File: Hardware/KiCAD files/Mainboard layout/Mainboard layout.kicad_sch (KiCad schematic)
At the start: 104 parts, among them J1 Conn_01x02, J10 Conn_01x02, J14 Conn_01x03, J15 Conn_01x03, J2 Conn_01x06, J28 Conn_01x03, J3 Conn_01x02, J30 USB-A1VSB6, J31 JST_03, J33 Conn_01x04, J34 JST_03, J35 JST_03, J36 JST_03, J37 JST_03, J38 JST_03, J39 JST_03, J4 Conn_01x06, J5 Conn_01x04, J6 Conn_01x06, J7 Conn_01x06, J8 Conn_01x06, J9 Conn_01x10, Q2 2DD1664, Q4 2N7000, SW8 Push_Button, SW9 Push_Button, U10 DRV8825PWPR, U12 ESP32-S3-WROOM-1, U3 PCA9534PW, U4 DRV8825PWPR, U8 DRV8825PWPR, U9 DRV8825PWPR

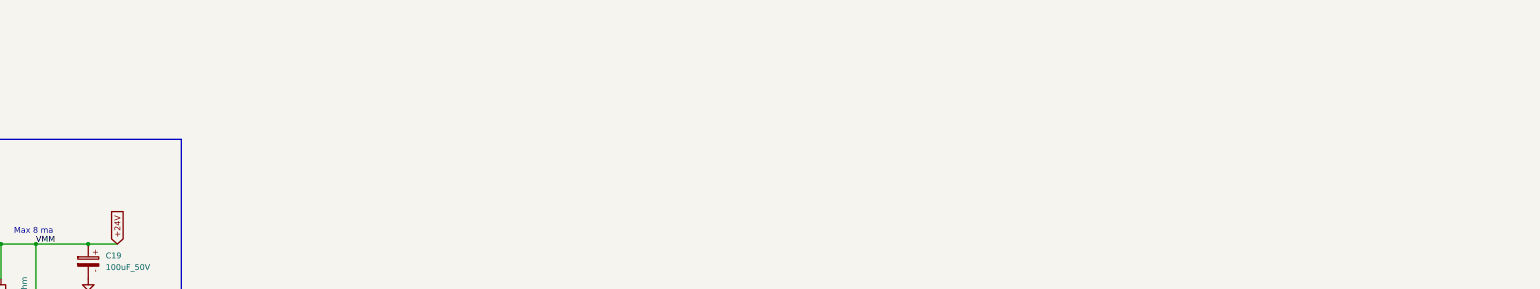
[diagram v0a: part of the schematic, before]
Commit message: Layout start
Was having issues with assigning pinouts on my initial schematics due to missing footprints, layouts broken into different schematics.
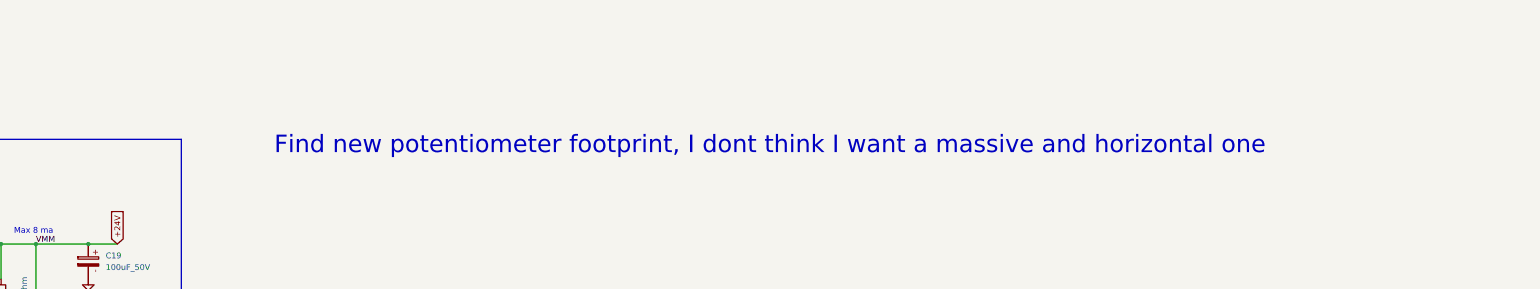
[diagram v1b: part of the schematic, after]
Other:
- note added: "Find new potentiometer footprint, I dont think I want a massive and horizontal one"
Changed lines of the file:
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@@
+		)
+	)
+	(text "Find new potentiometer footprint, I dont think I want a massive and horizontal one"
+		(exclude_from_sim no)
+		(at 480.314 294.64 0)
+		(effects
+			(font
+				(size 3.81 3.81)
+			)
 		)
 	)

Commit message: Mainboard Layout V1
completed Mainboard V1 layout and one swapping side, a hotfix to come of the other board to take swapping side
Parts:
- removed C10, C11, C13, C14, C15, C31, C32, C36, C39, C40, C44, C9: 0.1uF, PCM_SparkFun-Capacitor:C_0603_1608Metric, symbol PCM_SparkFun-Capacitor:0.1uF_0603_100V_10%
- removed C12, C19, C37, C45: 100uF_50V, Capacitor_THT:CP_Radial_D8.0mm_P3.50mm, symbol PCM_SL_Capacitors:100uF_50V
- removed C17, C18, C30, C38: 4.7uF, PCM_SparkFun-Capacitor:C_0603_1608Metric, symbol PCM_SparkFun-Capacitor:4.7uF_0603_35V_20%
- removed C20, C27, C33, C41: 470nF, PCM_SparkFun-Capacitor:C_0402_1005Metric, symbol PCM_SparkFun-Capacitor:470nF_0402_25V_10%
- removed C21, C28, C34, C42: 10nF, PCM_SparkFun-Capacitor:C_0603_1608Metric, symbol PCM_SparkFun-Capacitor:10nF_0603_50V_10%
- removed C22, C29, C35, C43: 0.1uF, PCM_SparkFun-Capacitor:C_0603_1608Metric, symbol PCM_SparkFun-Capacitor:0.1uF_0603_25V_20%
- removed J2, J4, J6, J7: Conn_01x06, PCM_SparkFun-Connector:1x06_P2.54mm, symbol PCM_SparkFun-Connector:Conn_01x06_P2.54mm
- removed J3: Conn_01x02, PCM_SparkFun-Connector:1x02_P2.54mm, symbol PCM_SparkFun-Connector:Conn_01x02_P2.54mm
- removed J33: Conn_01x04, PCM_SparkFun-Connector:1x04_P2.54mm, symbol PCM_SparkFun-Connector:Conn_01x04_P2.54mm
- removed Q4: 2N7000, PCM_Package_TO_SOT_THT_AKL:TO-92_Inline_Wide_SGD, symbol PCM_Transistor_MOSFET_AKL:2N7000
- removed R10, R19, R24, R29: 1.5k, PCM_SparkFun-Resistor:R_0603_1608Metric, symbol PCM_SparkFun-Resistor:1.5k_0603
- removed R11, R21, R26, R31: 10k Linear, PCM_SparkFun-Resistor:Bourns-PDB18, symbol PCM_SparkFun-Resistor:Trimpot_10k_RA_PTH
- removed R12, R22, R27, R32: 10k, PCM_SparkFun-Resistor:R_0603_1608Metric, symbol PCM_SparkFun-Resistor:10k_0603
- removed R16, R20, R25, R30: 1_Mohm, symbol PCM_Resistor_AKL:R_Generic
- removed R23, R28, R4, R9: .2 ohm, symbol PCM_Resistor_AKL:R_Generic
- removed R37, R38: 10k, Resistor_THT:R_Axial_DIN0207_L6.3mm_D2.5mm_P10.16mm_Horizontal, symbol PCM_SL_Resistors:10k
- removed U10, U4, U8, U9: DRV8825PWPR, symbol DRV8825PRPR driver chip:DRV8825PWPR
- added C23: 0.1uF, PCM_SparkFun-Capacitor:C_0603_1608Metric, symbol PCM_SparkFun-Capacitor:0.1uF_0603_25V_20%
- added J11, J17, J19, J21, J23, J24, J25, J26: Conn_01x06, PCM_SparkFun-Connector:1x06_P2.54mm, symbol PCM_SparkFun-Connector:Conn_01x06_P2.54mm
- added J12, J4, J6, J7: JST_06, Connector_JST:JST_EH_B6B-EH-A_1x06_P2.50mm_Vertical, symbol PCM_SL_Connectors:JST_06
- added J13: Conn_01x08, PCM_SparkFun-Connector:1x08_P2.54mm, symbol PCM_SparkFun-Connector:Conn_01x08_P2.54mm
- added J2: Screw_Terminal_2_P5.00mm, TerminalBlock_Phoenix:TerminalBlock_Phoenix_PT-1,5-2-5.0-H_1x02_P5.00mm_Horizontal, symbol PCM_SL_Screw_Terminal:Screw_Terminal_2_P5.00mm
- added J22, J29: Conn_01x03, PCM_SparkFun-Connector:1x03_P2.54mm, symbol PCM_SparkFun-Connector:Conn_01x03_P2.54mm
- added J3: Screw_Terminal_2_P3.50mm, TerminalBlock_Phoenix:TerminalBlock_Phoenix_PT-1,5-2-3.5-H_1x02_P3.50mm_Horizontal, symbol PCM_SL_Screw_Terminal:Screw_Terminal_2_P3.50mm
- added Q5: 2N7000, PCM_Package_TO_SOT_THT_AKL:TO-92_Inline_Wide_SGD, symbol PCM_Transistor_MOSFET_AKL:2N7000
- added R1: 1k, Resistor_THT:R_Axial_DIN0207_L6.3mm_D2.5mm_P10.16mm_Horizontal, symbol PCM_SL_Resistors:1k
- added R39: 10k, Resistor_THT:R_Axial_DIN0207_L6.3mm_D2.5mm_P10.16mm_Horizontal, symbol PCM_SL_Resistors:10k
- added R40: 100k, Resistor_THT:R_Axial_DIN0207_L6.3mm_D2.5mm_P10.16mm_Horizontal, symbol PCM_SL_Resistors:10k
- added R54: 10k, PCM_SparkFun-Resistor:R_0603_1608Metric, symbol PCM_SparkFun-Resistor:10k_0603
- added U5: PCA9534PW, PCM_SparkFun-Semiconductor-Standard:TSSOP-16_4.4x5mm_P0.65mm, symbol PCM_SparkFun-IC-Special-Function:PCA9534PW
- J1: value Conn_01x02 -> Programmer pins Conn_01x02
- J30: footprint USB-A1VSB6:ONSHORE_USB-A1VSB6 -> Connector_USB:USB_A_Kycon_KUSBX-AS1N-B_Horizontal
- R107, R89, R90, R91: footprint Resistor_SMD:R_0402_1005Metric_Wbry -> PCM_SparkFun-Resistor:R_0603_1608Metric
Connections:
- net SPI4_SCK is gone; now on net SPI4_CLK: J8.1 (Pin_1)
- net VBUS is gone; now on net +5V_HIGHPW: J30.1 (VUSB)
- net +24V: now also J2.1, J22.3 (Pin_3), J29.3 (Pin_3)
- net +3.3V: now also C23.1, J13.3 (Pin_3), J22.1 (Pin_1), Q5.2 (G), R54.1, U5.8 (VSS)
- net +5V: now also R40.2
- net DRIVER_0_STEP: now also J23.2 (Pin_2), J24.2 (Pin_2), J25.2 (Pin_2), J26.2 (Pin_2), R1.1
- net GND: now also C23.2, J13.2 (Pin_2), J2.2, J22.2 (Pin_2), J29.2 (Pin_2), J3.2, R39.2, U5.1 (A0), U5.16 (VDD), U5.2 (A1); no longer U12.15 (GPIO3/TOUCH3/ADC1_CH2)
- net IO_Interupter: now also U5.13 (~{INT})
- net MISO_1: now also J13.7 (Pin_7); no longer J5.2 (Pin_2)
- net MODE_0_GPIO: now also U3.4 (IO0), J23.5 (Pin_5), J24.5 (Pin_5), J25.5 (Pin_5); no longer U3.6 (IO2)
- net MODE_0_GPIOE: now also J26.5 (Pin_5)
- net MODE_1_GPIO: now also J23.4 (Pin_4), J24.4 (Pin_4), J25.4 (Pin_4)
- net MODE_1_GPIOE: now also J26.4 (Pin_4)
- net MODE_2_GPIO: now also U3.6 (IO2), J23.3 (Pin_3), J24.3 (Pin_3), J25.3 (Pin_3); no longer U3.4 (IO0)
- net MODE_2_GPIOE: now also J26.3 (Pin_3)
- net N_ENBL: now also J23.6 (Pin_6), J24.6 (Pin_6), J25.6 (Pin_6), J26.6 (Pin_6)
- net SPI1_CLK: now also J13.4 (Pin_4)
- net SPI1_CS: now also J13.6 (Pin_6)
- net SSR_Switch: now also J3.1, Q5.3 (D), R40.1
- net TEMP_HOTPLATE: no longer U12.39 (GPIO1/TOUCH1/ADC1_CH0)
- net TX: now reaches J1.1 (Pin_1), U12.37 (U0TXD/GPIO43/CLK_OUT1)
- net RX: now reaches J1.2 (Pin_2), U12.36 (U0RXD/GPIO44/CLK_OUT2)
- net at R53.1, U12.8 (GPIO15/U0RTS/ADC2_CH4/XTAL_32K_P), U3.15 (SDA): now also U5.15 (SDA)
- net at R52.1, U12.9 (GPIO16/U0CTS/ADC2_CH5/XTAL_32K_N), U3.14 (SCL): now also U5.14 (SCL)
- net DRDY_ALOW: now reaches U12.34 (MTDI/GPIO41/CLK_OUT1)
- net DRDY_ALOW: now also J13.8 (Pin_8)
- net TFT_interrupt: now reaches U12.35 (MTMS/GPIO42)
- net DIR: no longer names the net of U12.16 (GPIO46)
- new net: R54.2, U5.3 (A2)
- new net +12V: J29.1 (Pin_1)
- new net 3.3V_in1: Q5.1 (S), R39.1, U12.15 (GPIO3/TOUCH3/ADC1_CH2)
- new net A1_DRV0: J11.6 (Pin_6), J4.6
- new net A1_DRV1: J17.6 (Pin_6), J6.6
- new net A1_DRV2: J19.6 (Pin_6), J7.6
- new net A1_DRV3: J12.6, J21.6 (Pin_6)
- new net A2_DRV0: J11.3 (Pin_3), J4.3
- new net A2_DRV1: J17.3 (Pin_3), J6.3
- new net A2_DRV2: J19.3 (Pin_3), J7.3
- new net A2_DRV3: J12.3, J21.3 (Pin_3)
- new net B1_DRV0: J11.4 (Pin_4), J4.4
- new net B1_DRV1: J17.4 (Pin_4), J6.4
- new net B1_DRV2: J19.4 (Pin_4), J7.4
- new net B1_DRV3: J12.4, J21.4 (Pin_4)
- new net B2_DRV0: J11.1 (Pin_1), J4.1
- new net B2_DRV1: J17.1 (Pin_1), J6.1
- new net B2_DRV2: J19.1 (Pin_1), J7.1
- new net B2_DRV3: J12.1, J21.1 (Pin_1)
- new net CHAINL0_MISO_1: J13.5 (Pin_5), J5.2 (Pin_2)
- new net DIR0: J23.1 (Pin_1), U5.4 (IO0)
- new net DIR1: J24.1 (Pin_1), U5.5 (IO1)
- new net DIR2: J25.1 (Pin_1), U5.6 (IO2)
- new net DIR3: J26.1 (Pin_1), U5.7 (IO3)
- new net STEP: R1.2
- no-connect marks 31 -> 28
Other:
- note added: "may want to have parralel interrupts"
- note removed: "A1-A2, B1-B2 phases for stepper motors"
- note removed: "ALL NOTES FOR MOTOR DRIVER SCHEM"
- note removed: "DRV8825 1.1 D0"
- note removed: "DRV8825 1.1 D02"
- note removed: "DRV8825 1.1 D03 Extruder"
- note removed: "DRV8825 1.1 D1"
- note removed: "Find new potentiometer footprint, I dont think I want a massive and horizontal one"
- note removed: "Max 8 ma"
- note removed: "NoteMeausure impedance of the lines in layout ISA and ISB are .20 ohm, do with wire parasitics"
- note removed: "Replace all generics for specific componenets"
- note removed: "SLP @ fault"
- note removed: "This is designed to be integrated only leaving a connector output to the stepper"
- note removed: "Verify the coil Physically"
- moved on the sheet: J14, J15, J28

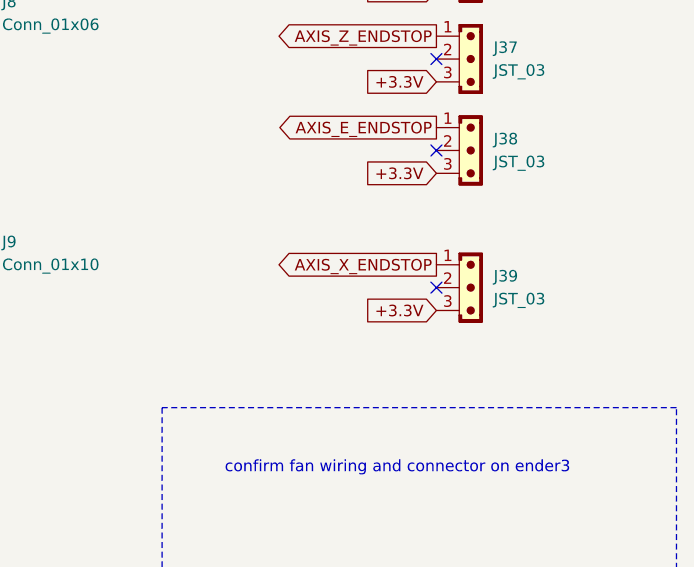
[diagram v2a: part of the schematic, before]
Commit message: Hotfix to create non-swapping board
hotfix on non-swapping done, swapping board is mapped for completion after CAD modeling phase begins
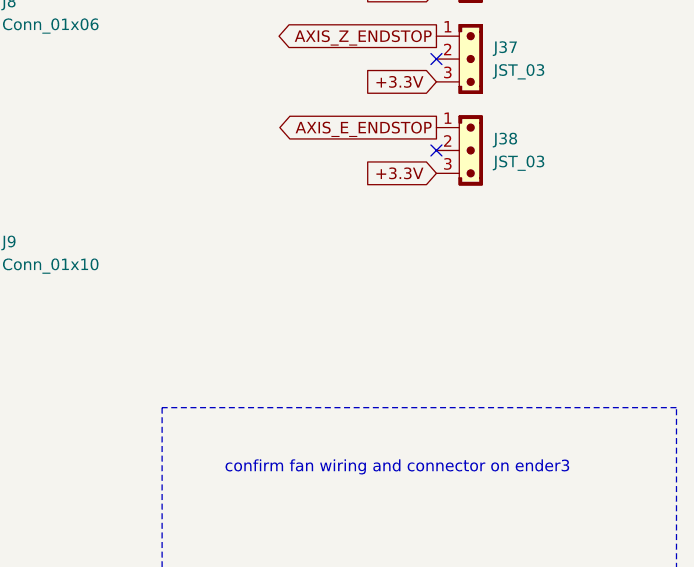
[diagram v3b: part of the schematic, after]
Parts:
- removed J39: JST_03, Connector_JST:JST_EH_B3B-EH-A_1x03_P2.50mm_Vertical, symbol PCM_SL_Connectors:JST_03
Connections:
- no-connect marks 28 -> 27
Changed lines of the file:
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@@
 	)
 	(no_connect
-		(at 797.56 91.44)
-	)
-	(no_connect
 		(at 797.56 45.72)
 	)
@@
 		)
 	)
-	(global_label "AXIS_X_ENDSTOP"
-		(shape output)
-		(at 797.56 88.9 180)
-		(fields_autoplaced yes)
-		(effects
-			(font
-				(size 1.27 1.27)
-			)
-			(justify right)
-		)
-		(property "Intersheetrefs" "${INTERSHEET_REFS}"
-			(at 778.7906 88.9 0)
-			(hide yes)
-			(show_name no)
-			(do_not_autoplace no)
-			(effects
-				(font
-					(size 1.27 1.27)
-				)
-				(justify right)
-			)
-		)
-	)
 	(global_label "SSR_Switch"
 		(shape input)
@@
 		)
 	)
-	(global_label "+3.3V"
-		(shape input)
-		(at 797.56 93.98 180)
-		(fields_autoplaced yes)
-		(effects
-			(font
-				(size 1.27 1.27)
-			)
-			(justify right)
-		)
-		(property "Intersheetrefs" "${INTERSHEET_REFS}"
-			(at 788.89 93.98 0)
-			(hide yes)
-			(show_name no)
-			(do_not_autoplace no)
-			(effects
-				(font
-					(size 1.27 1.27)
-				)
-				(justify right)
-			)
-		)
-	)
 	(global_label "MODE_2_GPIO"
 		(shape input)
@@
 					(unit 1)
 				)
-			)
-		)
-	)
-	(symbol
-		(lib_id "PCM_SL_Connectors:JST_03")
-		(at 801.37 91.44 0)
-		(unit 1)
-		(body_style 1)
-		(exclude_from_sim no)
-		(in_bom yes)
-		(on_board yes)
-		(in_pos_files yes)
-		(dnp no)
-		(property "Reference" "J39"
-			(at 803.91 90.1699 0)
-			(show_name no)
-			(do_not_autoplace no)
-			(effects
-				(font
-					(size 1.27 1.27)
-				)
-				(justify left)
-			)
-		)
-		(property "Value" "JST_03"
-			(at 803.91 92.7099 0)
-			(show_name no)
-			(do_not_autoplace no)
-			(effects
-				(font
-					(size 1.27 1.27)
-				)
-				(justify left)
-			)
-		)
-		(property "Footprint" "Connector_JST:JST_EH_B3B-EH-A_1x03_P2.50mm_Vertical"
-			(at 801.37 83.82 0)
-			(hide yes)
-			(show_name no)
-			(do_not_autoplace no)
-			(effects
-				(font
-					(size 1.27 1.27)
-				)
-			)
-		)
-		(property "Datasheet" ""
-			(at 801.37 83.82 0)
-			(hide yes)
-			(show_name no)
-			(do_not_autoplace no)
-			(effects
-				(font
-					(size 1.27 1.27)
-				)
-			)
-		)
-		(property "Description" "JST Connector  3 pins"
-			(at 801.37 91.44 0)
-			(hide yes)
-			(show_name no)
-			(do_not_autoplace no)
-			(effects
-				(font
-					(size 1.27 1.27)
-				)
-			)
-		)
-		(pin "2"
-		)
-		(pin "1"
-		)
-		(pin "3"
-		)
-		(instances
-			(project "Mainboard layout"
-				(path "/322d2c9f-d9a6-40cc-b638-389f55be9478"
-					(reference "J39")
-					(unit 1)
-				)

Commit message: another hotfix to the board, little adjustments
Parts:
- added R56: 10k, PCM_SparkFun-Resistor:R_0603_1608Metric, symbol PCM_SparkFun-Resistor:10k_0603
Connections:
- net +3.3V: now also R56.2
- net StepE: now reaches U12.39 (GPIO1/TOUCH1/ADC1_CH0)
- net StepE: now also R56.1
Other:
- note added: "Not in layout"
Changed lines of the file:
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@@
 	(text "reset"
 		(exclude_from_sim no)
-		(at 183.134 21.082 0)
+		(at 185.166 25.146 0)
 		(effects
 			(font
@@
 		)
 	)
+	(text "Not in layout "
+		(exclude_from_sim no)
+		(at 302.26 67.564 0)
+		(effects
+			(font
+				(size 1.27 1.27)
+			)
+		)
+	)
 	(text "verify that esp interrupt is on this pin\n"
 		(exclude_from_sim no)
@@
 	)
 	(junction
+		(at 317.5 67.31)
+		(diameter 0)
+		(color 0 0 0 0)
+	)
+	(junction
 		(at 118.11 38.1)
 		(diameter 0)
@@
 	(wire
 		(pts
+			(xy 320.04 67.31) (xy 317.5 67.31)
+		)
+		(stroke
+			(width 0)
+			(type default)
+		)
+	)
+	(wire
+		(pts
 			(xy 246.38 90.17) (xy 304.8 90.17)
 		)
@@
 	(wire
 		(pts
+			(xy 311.15 67.31) (xy 317.5 67.31)
+		)
+		(stroke
+			(width 0)
+			(type default)
+		)
+	)
+	(wire
+		(pts
 			(xy 40.005 200.66) (xy 40.005 196.85)
 		)
@@
 	(wire
 		(pts
+			(xy 246.38 69.85) (xy 311.15 69.85)
+		)
+		(stroke
+			(width 0)
+			(type default)
+		)
+	)
+	(wire
+		(pts
 			(xy 154.94 59.69) (xy 142.24 59.69)
 		)
@@
 	(wire
 		(pts
+			(xy 311.15 69.85) (xy 311.15 67.31)
+		)
+		(stroke
+			(width 0)
+			(type default)
+		)
+	)
+	(wire
+		(pts
 			(xy 246.38 67.31) (xy 271.78 67.31)
 		)
@@
 	(wire
 		(pts
+			(xy 317.5 72.39) (xy 317.5 67.31)
+		)
+		(stroke
+			(width 0)
+			(type default)
+		)
+	)
+	(wire
+		(pts
 			(xy 90.17 124.46) (xy 92.71 124.46)
 		)
@@
 		)
 	)
-	(global_label "TEMP_HOTPLATE"
-		(shape input)
-		(at 288.29 68.58 0)
-		(fields_autoplaced yes)
-		(effects
-			(font
-				(size 1.27 1.27)
-			)
-			(justify left)
-		)
-		(property "Intersheetrefs" "${INTERSHEET_REFS}"
-			(at 306.2127 68.58 0)
-			(hide yes)
-			(show_name no)
-			(do_not_autoplace no)
-			(effects
-				(font
-					(size 1.27 1.27)
-				)
-				(justify left)
-			)
-		)
-	)
 	(global_label "DIR0"
 		(shape input)
@@
 		)
 	)
+	(global_label "+3.3V"
+		(shape input)
+		(at 325.12 67.31 0)
+		(fields_autoplaced yes)
+		(effects
+			(font
+				(size 1.27 1.27)
+			)
+			(justify left)
+		)
+		(property "Intersheetrefs" "${INTERSHEET_REFS}"
+			(at 333.79 67.31 0)
+			(hide yes)
+			(show_name no)
+			(do_not_autoplace no)
+			(effects
+				(font
+					(size 1.27 1.27)
+				)
+				(justify left)
+			)
+		)
+	)
 	(global_label "DATA_SELECT"
 		(shape output)
@@
 		)
 	)
+	(global_label "StepE"
+		(shape output)
+		(at 317.5 72.39 270)
+		(fields_autoplaced yes)
+		(effects
+			(font
+				(size 1.27 1.27)
+			)
+			(justify right)
+		)
+		(property "Intersheetrefs" "${INTERSHEET_REFS}"
+			(at 317.5 80.697 90)
+			(hide yes)
+			(show_name no)
+			(do_not_autoplace no)
+			(effects
+				(font
+					(size 1.27 1.27)
+				)
+				(justify right)
+			)
+		)
+	)
 	(global_label "MOSI_1"
 		(shape input)
@@
 					(unit 1)
 				)
+			)
+		)
+	)
+	(symbol
+		(lib_id "PCM_SparkFun-Resistor:10k_0603")
+		(at 322.58 67.31 0)
+		(mirror x)
+		(unit 1)
+		(body_style 1)
+		(exclude_from_sim no)
+		(in_bom yes)
+		(on_board yes)
+		(in_pos_files yes)
+		(dnp no)
+		(fields_autoplaced yes)
+		(property "Reference" "R56"
+			(at 323.8501 64.77 90)
+			(show_name no)
+			(do_not_autoplace no)
+			(effects
+				(font
+					(size 1.27 1.27)
+				)
+				(justify right)
+			)
+		)
+		(property "Value" "10k"
+			(at 321.3101 64.77 90)
+			(show_name no)
+			(do_not_autoplace no)
+			(effects
+				(font
+					(size 1.27 1.27)
+				)
+				(justify right)
+			)
+		)
+		(property "Footprint" "PCM_SparkFun-Resistor:R_0603_1608Metric"
+			(at 322.58 62.992 0)
+			(hide yes)
+			(show_name no)
+			(do_not_autoplace no)
+			(effects
+				(font
+					(size 1.27 1.27)
+				)
+			)
+		)
+		(property "Datasheet" "https://www.vishay.com/docs/20035/dcrcwe3.pdf"
+			(at 322.58 58.42 0)
+			(hide yes)
+			(show_name no)
+			(do_not_autoplace no)
+			(effects
+				(font
+					(size 1.27 1.27)
+				)
+			)
+		)
+		(property "Description" "Resistor"
+			(at 322.58 55.88 0)
+			(hide yes)
+			(show_name no)
+			(do_not_autoplace no)
+			(effects
+				(font
+					(size 1.27 1.27)
+				)
+			)
+		)
+		(property "PROD_ID" "RES-00824"
+			(at 322.58 60.96 0)
+			(hide yes)
+			(show_name no)
+			(do_not_autoplace no)
+			(effects
+				(font
+					(size 1.27 1.27)
+				)
+			)
+		)
+		(pin "1"
+		)
+		(pin "2"
+		)
+		(instances
+			(project "Mainboard layout"
+				(path "/322d2c9f-d9a6-40cc-b638-389f55be9478"
+					(reference "R56")
+					(unit 1)
+				)

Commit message: 1st push of PCB's for printing
This is pre-peer review. This almost certainly has section that need adjustment. also realized I'm missing the USB-Uart bridge. first thing added in next version.
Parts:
- removed J1: Programmer pins Conn_01x02, PCM_SparkFun-Connector:1x02_P2.54mm, symbol PCM_SparkFun-Connector:Conn_01x02_P2.54mm
- removed J11, J17, J19, J21, J23, J24, J25, J26: Conn_01x06, PCM_SparkFun-Connector:1x06_P2.54mm, symbol PCM_SparkFun-Connector:Conn_01x06_P2.54mm
- removed J14, J15, J22, J28, J29: Conn_01x03, PCM_SparkFun-Connector:1x03_P2.54mm, symbol PCM_SparkFun-Connector:Conn_01x03_P2.54mm
- removed Q5: 2N7000, PCM_Package_TO_SOT_THT_AKL:TO-92_Inline_Wide_SGD, symbol PCM_Transistor_MOSFET_AKL:2N7000
- removed R51: 10k, PCM_SparkFun-Resistor:R_0603_1608Metric, symbol PCM_SparkFun-Resistor:10k_0603
- added C3: 0.1uF, PCM_SparkFun-Capacitor:C_0603_1608Metric, symbol PCM_SparkFun-Capacitor:0.1uF_0603_25V_20%
- added C4: 10uF, PCM_SparkFun-Capacitor:C_1210_3225Metric, symbol PCM_SparkFun-Capacitor:10uF_1210_50V_20%
- added J1: MSD-1-A, CONN9_MSD-1_CUD, symbol 2026-04-18_00-57-23:MSD-1-A
- added J11, J25, J26, J27: Conn_01x04, PCM_SparkFun-Connector:1x04_P2.54mm, symbol PCM_SparkFun-Connector:Conn_01x04_P2.54mm
- added J17, J18, J19, J20, J22, J23, J24, J28: PINHD_1x8_Male, Connector_PinHeader_2.54mm:PinHeader_1x08_P2.54mm_Vertical, symbol PCM_SL_Pin_Headers:PINHD_1x8_Male
- added Q1: BS170, PCM_Package_TO_SOT_THT_AKL:TO-92_Inline_Wide_DGS, symbol PCM_Transistor_MOSFET_AKL:BS170
- added R2: 50 ohmR_0805, PCM_Resistor_SMD_AKL:R_0805_2012Metric, symbol PCM_Resistor_AKL:R_0805
- added R3, R4: 100, PCM_SparkFun-Resistor:R_0603_1608Metric, symbol PCM_SparkFun-Resistor:100_0603
- added R7: 50 ohm R_0805, PCM_Resistor_SMD_AKL:R_0805_2012Metric, symbol PCM_Resistor_AKL:R_0805
- R50: value 10k -> 1k
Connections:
- net +12V: now also J11.1 (Pin_1), J17.1, J18.1, J19.1, J20.1
- net +24V: now also J5.3 (Pin_3), J11.3 (Pin_3), J25.3 (Pin_3), J26.3 (Pin_3), J27.3 (Pin_3)
- net +3.3V: now also J5.1 (Pin_1), R54.2, U3.16 (VDD), J1.4 (VDD), J26.1 (Pin_1), Q1.2 (G); no longer R54.1, U3.8 (VSS), U5.8 (VSS)
- net +5V: now also J27.1 (Pin_1)
- net +5V_HIGHPW: now also J25.1 (Pin_1)
- net 3.3V_in1: now also Q1.3 (S)
- net A1_DRV0: now also J20.5
- net A1_DRV1: now also J17.5
- net A1_DRV2: now also J18.5
- net A2_DRV0: now also J20.6
- net A2_DRV1: now also J17.6
- net A2_DRV2: now also J18.6
- net B1_DRV0: now also J20.4
- net B1_DRV1: now also J17.4
- net B1_DRV2: now also J18.4
- net B2_DRV0: now also J20.3
- net B2_DRV1: now also J17.3
- net B2_DRV2: now also J18.3
- net CHAINL0_MISO_1: now also J1.7 (DAT0); no longer J5.2 (Pin_2)
- net DIR0: now also J23.8
- net DIR1: now also J22.8
- net DIR2: now also J24.8
- net DRIVER_0_STEP: now also J22.7, J23.7, J24.7, J28.7
- net GND: now also J5.2 (Pin_2), J5.4 (Pin_4), U3.3 (A2), U3.8 (VSS), U5.8 (VSS), C3.2, C4.2, J1.6 (VSS), J11.2 (Pin_2), J11.4 (Pin_4), J17.2, J17.8, J18.2, J18.8, J19.2, J19.8, J20.2, J20.8, J25.2 (Pin_2), J25.4 (Pin_4), J26.2 (Pin_2), J26.4 (Pin_4), J27.2 (Pin_2), J27.4 (Pin_4); no longer U3.16 (VDD), U5.16 (VDD)
- net MISO_1: now also R4.2; no longer U12.19 (GPIO11/TOUCH11/ADC2_CH0/FSPID/FSPIIO5/SUBSPID)
- net MISO_4: now also R3.2; no longer U12.30 (SPIDQS/GPIO37/FSPIQ/SUBSPIQ)
- net MODE_0_GPIO: now also J22.4, J23.4, J24.4
- net MODE_0_GPIOE: now also J28.4
- net MODE_1_GPIO: now also J22.3, J23.3, J24.3
- net MODE_1_GPIOE: now also J28.3
- net MODE_2_GPIO: now also J22.2, J23.2, J24.2
- net MODE_2_GPIOE: now also J28.2
- net MOSI_1: now also J1.3 (CMD); no longer J5.3 (Pin_3)
- net MOSI_4: now also U12.11 (GPIO18/U1RXD/ADC2_CH7/CLK_OUT3); no longer U12.28 (SPIIO6/GPIO35/FSPID/SUBSPID)
- net N_ENBL: now also J22.1, J23.1, J24.1, J28.1
- net SPI1_CLK: now also J1.5 (CLK); no longer J5.4 (Pin_4)
- net SPI1_CS: now also J1.2 (CD/DAT3); no longer J5.1 (Pin_1)
- net SPI4_CLK: now also U12.10 (GPIO17/U1TXD/ADC2_CH6); no longer U12.29 (SPIIO7/GPIO36/FSPICLK/SUBSPICLK)
- net SSR_Switch: now also Q1.1 (D)
- net at R53.1, U3.15 (SDA), U5.15 (SDA): now also R2.1; no longer U12.8 (GPIO15/U0RTS/ADC2_CH4/XTAL_32K_P)
- net at R52.1, U3.14 (SCL), U5.14 (SCL): now also R7.1; no longer U12.9 (GPIO16/U0CTS/ADC2_CH5/XTAL_32K_N)
- net at U5.3 (A2): now also R56.1; no longer R54.2
- net nSLP: now reaches U12.16 (GPIO46)
- net nSLP: now also J22.6, J23.6, J24.6, J28.6
- net at U12.22 (GPIO14/TOUCH14/ADC2_CH3/FSPIWP/FSPIDQS/SUBSPIWP): now also R3.1
- net at SW9.1, U12.27 (GPIO0/BOOT): now also C3.1
- net at SW8.1, U12.3 (EN): now also C4.1
- net A1_DRV3 renamed A1_DRVE
- net A1_DRVE: now also J19.5
- net A2_DRV3 renamed A2_DRVE
- net A2_DRVE: now also J19.6
- net B1_DRV3 renamed B1_DRVE
- net B1_DRVE: now also J19.4
- net B2_DRV3 renamed B2_DRVE
- net B2_DRVE: now also J19.3
- net DIR3 renamed DIRE
- net DIRE: now also J28.8
- net StepE renamed Reset
- net Reset: now also J22.5, J23.5, J24.5, J28.5; no longer R56.1
- new net: R7.2, U12.9 (GPIO16/U0CTS/ADC2_CH5/XTAL_32K_N)
- new net: R54.1, U5.16 (VDD)
- new net: R4.1, U12.19 (GPIO11/TOUCH11/ADC2_CH0/FSPID/FSPIIO5/SUBSPID)
- new net: R2.2, U12.8 (GPIO15/U0RTS/ADC2_CH4/XTAL_32K_P)
- new net nFault: J17.7, J18.7, J19.7, J20.7
- no-connect marks 27 -> 22
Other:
- note added: "change val"
- note removed: "Not in layout"
- note removed: "programmer pins"
- moved on the sheet: C16, C23, R54
